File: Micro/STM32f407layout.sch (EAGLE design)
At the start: 68 parts, among them Q1 ASF, Q2 ASV-8, T3 FDN340P, T4 AP1117_LIN_REG

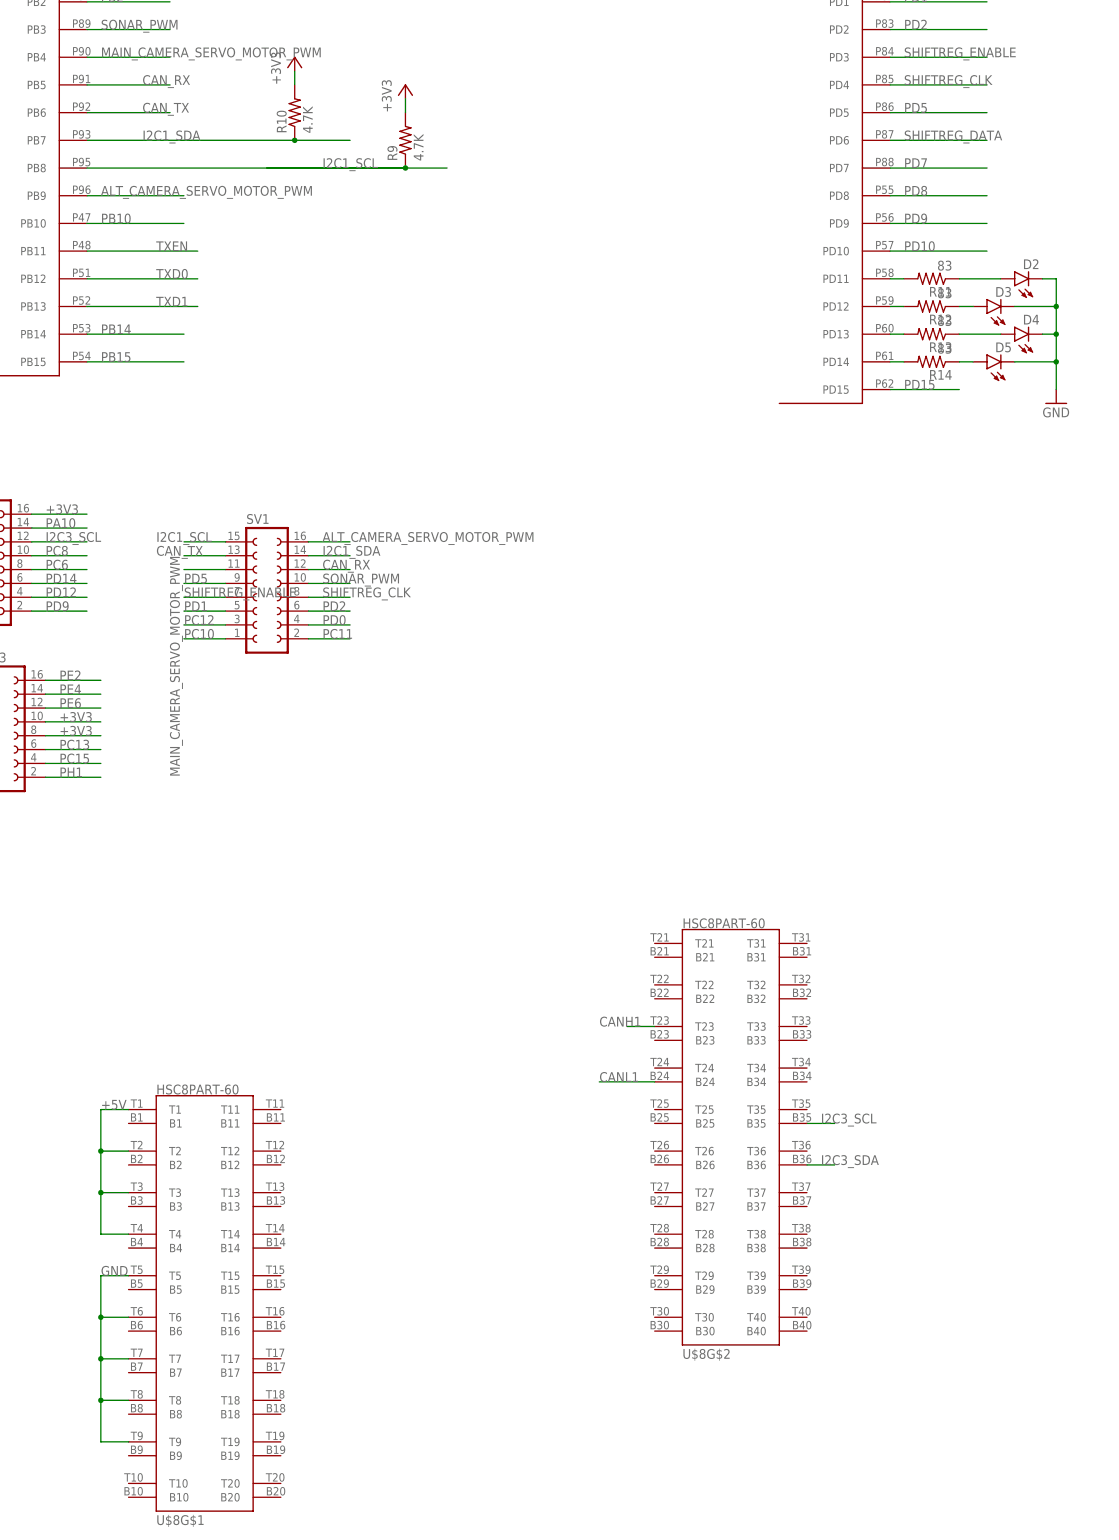
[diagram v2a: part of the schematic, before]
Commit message: Imprved spacing, changed bottom pinouts
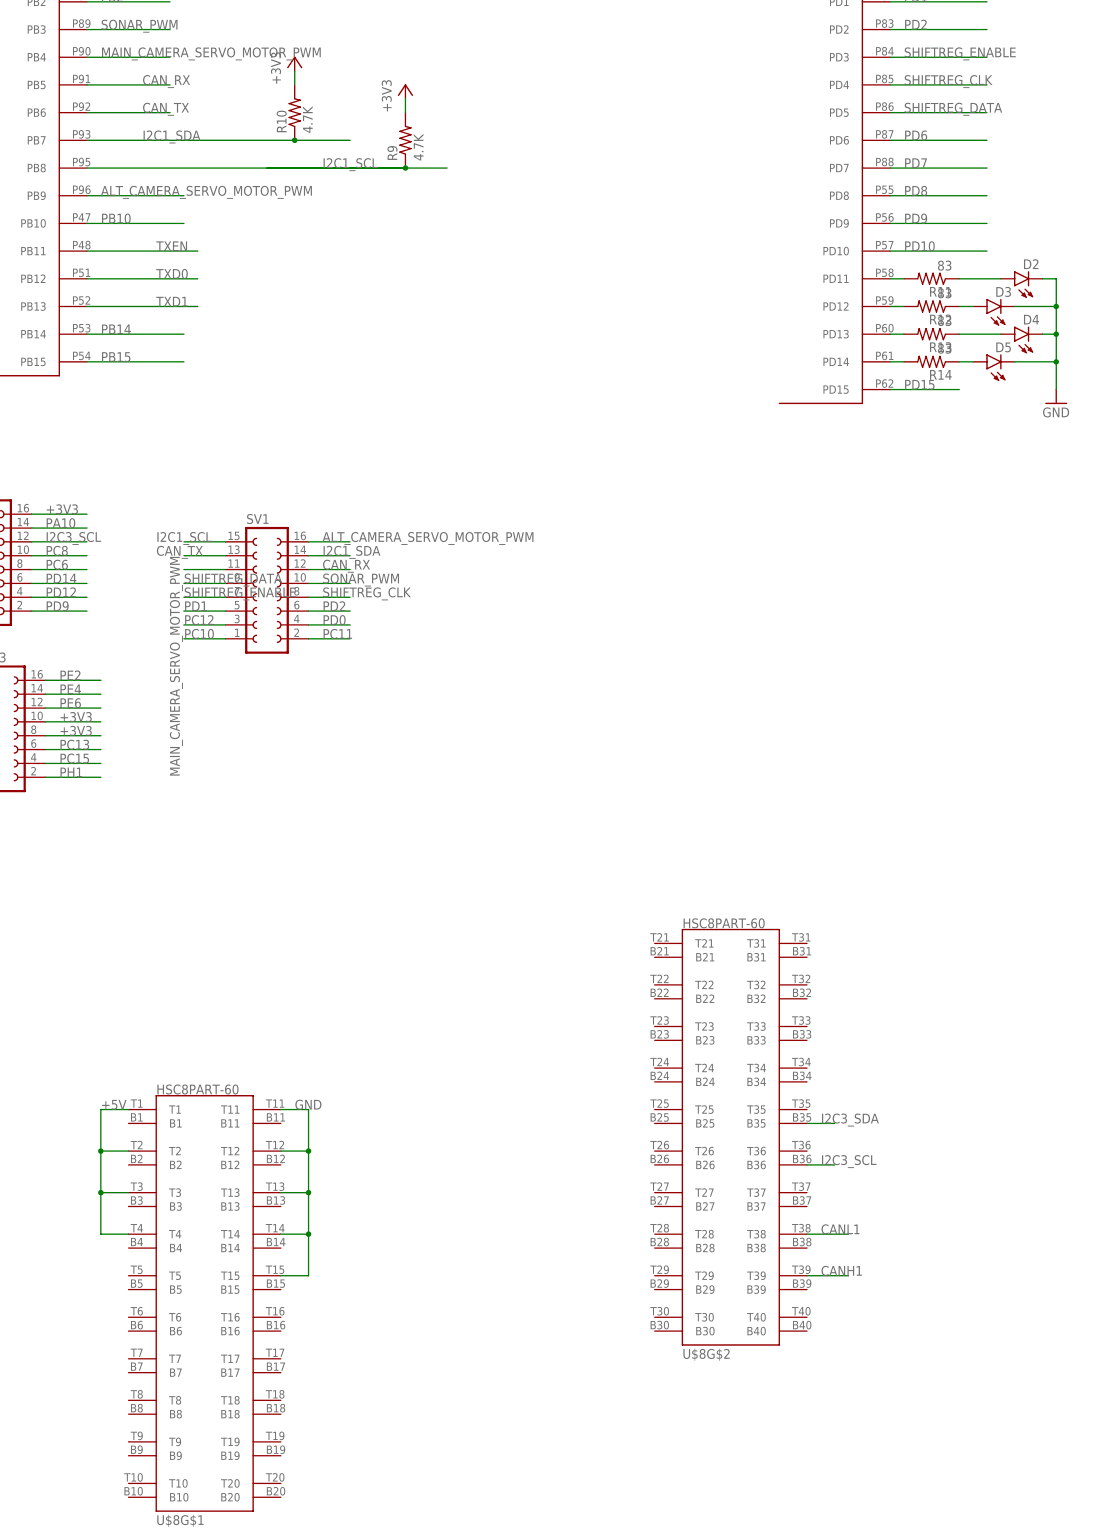
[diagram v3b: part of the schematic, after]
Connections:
- removed net PD5: SV1.9, U$1G$4.PD5
- new net PD6: U$1G$4.PD6
- net CANH1: now also U$8G$2.T39; no longer U$8G$2.T23
- net CANL1: now also U$8G$2.T38; no longer U$8G$2.B24
- net GND: now also U$8G$1.T11, U$8G$1.T12, U$8G$1.T13, U$8G$1.T14, U$8G$1.T15; no longer U$8G$1.T5, U$8G$1.T6, U$8G$1.T7, U$8G$1.T8, U$8G$1.T9
- net I2C3_SCL: now also U$8G$2.B36; no longer U$8G$2.B35
- net I2C3_SDA: now also U$8G$2.B35; no longer U$8G$2.B36
- net SHIFTREG_DATA: now also SV1.9, U$1G$4.PD5; no longer U$1G$4.PD6

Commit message: Fixed DRC Errors, Began fixing other problems
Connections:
- removed net PC11: SV1.2, U$1G$3.PC11
- new net TEMP_BACKUP: SV1.2, U$1G$3.PC11, U$8G$2.T25
- net +5V: now also U$8G$1.T5, U$8G$1.T6; no longer U$8G$1.T1, U$8G$1.T2
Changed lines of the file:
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@@
 </segment>
 <segment>
-<pinref part="U$8" gate="G$1" pin="T1"/>
-<wire x1="447.04" y1="139.7" x2="441.96" y2="139.7" width="0.1524" layer="91"/>
-<label x="441.96" y="139.7" size="1.778" layer="95"/>
-<wire x1="441.96" y1="139.7" x2="441.96" y2="132.08" width="0.1524" layer="91"/>
-<pinref part="U$8" gate="G$1" pin="T2"/>
-<wire x1="441.96" y1="132.08" x2="447.04" y2="132.08" width="0.1524" layer="91"/>
-<wire x1="441.96" y1="132.08" x2="441.96" y2="124.46" width="0.1524" layer="91"/>
-<junction x="441.96" y="132.08"/>
+<label x="441.96" y="124.46" size="1.778" layer="95"/>
 <pinref part="U$8" gate="G$1" pin="T3"/>
 <wire x1="441.96" y1="124.46" x2="447.04" y2="124.46" width="0.1524" layer="91"/>
 <wire x1="441.96" y1="124.46" x2="441.96" y2="116.84" width="0.1524" layer="91"/>
-<junction x="441.96" y="124.46"/>
 <pinref part="U$8" gate="G$1" pin="T4"/>
 <wire x1="441.96" y1="116.84" x2="447.04" y2="116.84" width="0.1524" layer="91"/>
+<wire x1="441.96" y1="116.84" x2="441.96" y2="109.22" width="0.1524" layer="91"/>
+<junction x="441.96" y="116.84"/>
+<pinref part="U$8" gate="G$1" pin="T5"/>
+<wire x1="441.96" y1="109.22" x2="447.04" y2="109.22" width="0.1524" layer="91"/>
+<wire x1="441.96" y1="109.22" x2="441.96" y2="101.6" width="0.1524" layer="91"/>
+<junction x="441.96" y="109.22"/>
+<pinref part="U$8" gate="G$1" pin="T6"/>
+<wire x1="441.96" y1="101.6" x2="447.04" y2="101.6" width="0.1524" layer="91"/>
 </segment>
 </net>
@@
 </segment>
 </net>
-<net name="PC11" class="0">
+<net name="TEMP_BACKUP" class="0">
 <segment>
 <pinref part="SV1" gate="G$1" pin="2"/>
@@
 <label x="586.74" y="454.66" size="1.778" layer="95"/>
 </segment>
-</net>
+<segment>
+<pinref part="U$8" gate="G$2" pin="T25"/>
+<wire x1="543.56" y1="139.7" x2="535.94" y2="139.7" width="0.1524" layer="91"/>
+<label x="528.32" y="139.7" size="1.778" layer="95"/>
+</segment>
+</net>

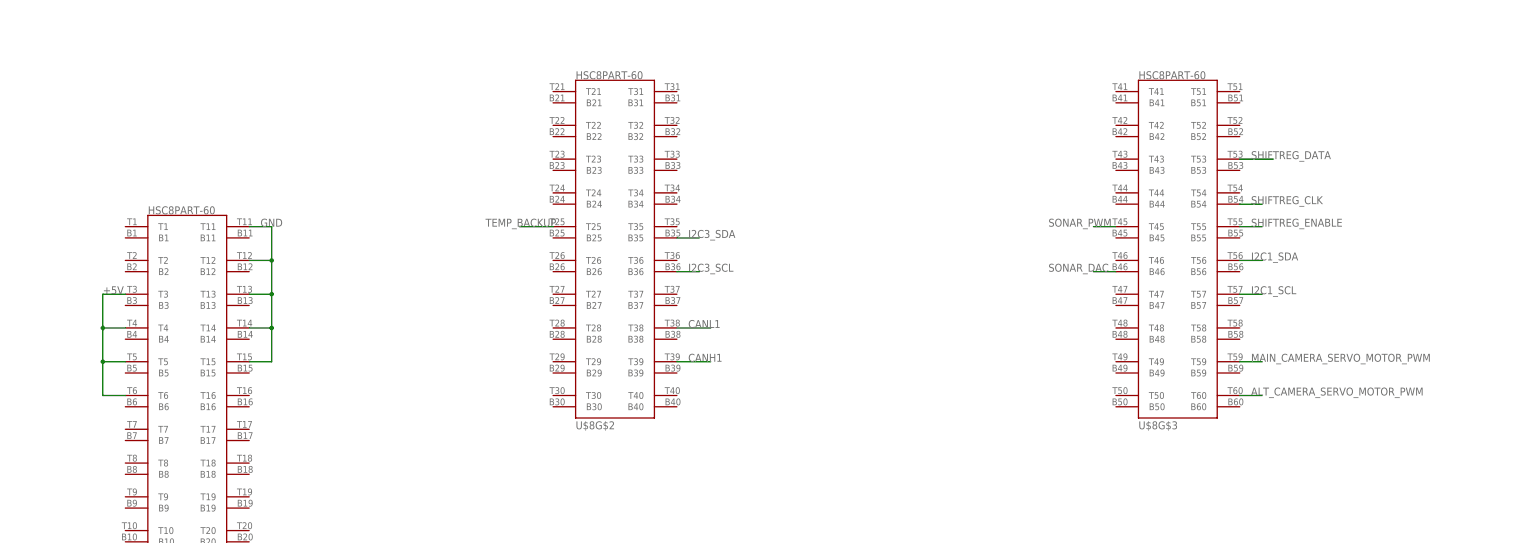
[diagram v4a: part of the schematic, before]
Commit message: Fixed some wiring on the microboard
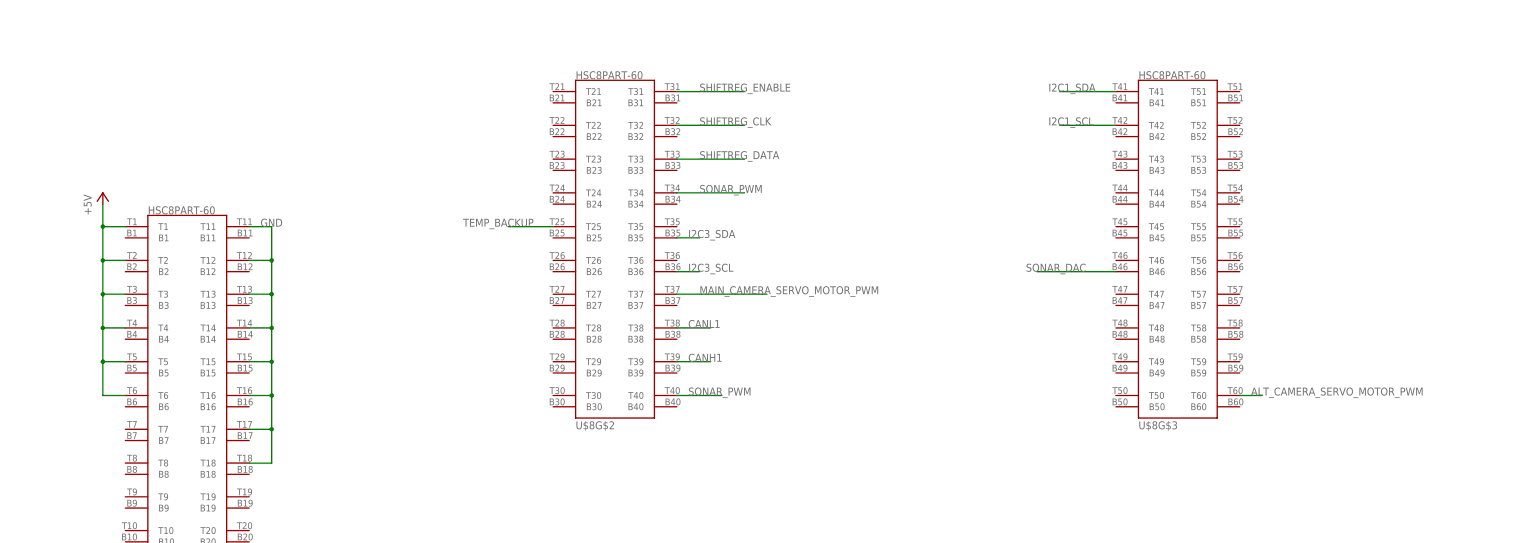
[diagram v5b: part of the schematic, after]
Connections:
- net +5V: now also U$8G$1.T1, U$8G$1.T2
- net GND: now also U$8G$1.T16, U$8G$1.T17, U$8G$1.T18
- net I2C1_SCL: now also U$8G$3.T42; no longer U$8G$3.T57
- net I2C1_SDA: now also U$8G$3.T41; no longer U$8G$3.T56
- net MAIN_CAMERA_SERVO_MOTOR_PWM: now also U$8G$2.T37; no longer U$8G$3.T59
- net SHIFTREG_CLK: now also U$8G$2.T32; no longer U$8G$3.B54
- net SHIFTREG_DATA: now also U$8G$2.T33; no longer U$8G$3.T53
- net SHIFTREG_ENABLE: now also U$8G$2.T31; no longer U$8G$3.T55
- net SONAR_PWM: now also U$8G$2.T34, U$8G$2.T40; no longer U$8G$3.T45
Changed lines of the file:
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@@
 <layers>
 <layer number="1" name="Top" color="4" fill="1" visible="no" active="no"/>
+<layer number="2" name="Route2" color="1" fill="3" visible="no" active="no"/>
+<layer number="3" name="Route3" color="4" fill="3" visible="no" active="no"/>
+<layer number="4" name="Route4" color="1" fill="4" visible="no" active="no"/>
+<layer number="5" name="Route5" color="4" fill="4" visible="no" active="no"/>
+<layer number="6" name="Route6" color="1" fill="8" visible="no" active="no"/>
+<layer number="7" name="Route7" color="4" fill="8" visible="no" active="no"/>
+<layer number="8" name="Route8" color="1" fill="2" visible="no" active="no"/>
+<layer number="9" name="Route9" color="4" fill="2" visible="no" active="no"/>
+<layer number="10" name="Route10" color="1" fill="7" visible="no" active="no"/>
+<layer number="11" name="Route11" color="4" fill="7" visible="no" active="no"/>
+<layer number="12" name="Route12" color="1" fill="5" visible="no" active="no"/>
+<layer number="13" name="Route13" color="4" fill="5" visible="no" active="no"/>
+<layer number="14" name="Route14" color="1" fill="6" visible="no" active="no"/>
+<layer number="15" name="Route15" color="4" fill="6" visible="no" active="no"/>
 <layer number="16" name="Bottom" color="1" fill="1" visible="no" active="no"/>
 <layer number="17" name="Pads" color="2" fill="1" visible="no" active="no"/>
@@
 <part name="+3V20" library="supply1" deviceset="+3V3" device=""/>
 <part name="U$8" library="Connectors" deviceset="HSC8PART-60" device=""/>
+<part name="P+1" library="supply1" deviceset="+5V" device=""/>
 </parts>
 <sheets>
@@
 <instance part="U$8" gate="G$2" x="556.26" y="134.62"/>
 <instance part="U$8" gate="G$3" x="683.26" y="134.62"/>
+<instance part="P+1" gate="1" x="441.96" y="147.32"/>
 </instances>
 <busses>
@@
 <junction x="480.06" y="116.84"/>
 <label x="477.52" y="139.7" size="1.778" layer="95"/>
+<wire x1="480.06" y1="109.22" x2="480.06" y2="101.6" width="0.1524" layer="91"/>
+<junction x="480.06" y="109.22"/>
+<pinref part="U$8" gate="G$1" pin="T16"/>
+<wire x1="480.06" y1="101.6" x2="474.98" y2="101.6" width="0.1524" layer="91"/>
+<wire x1="480.06" y1="101.6" x2="480.06" y2="93.98" width="0.1524" layer="91"/>
+<junction x="480.06" y="101.6"/>
+<pinref part="U$8" gate="G$1" pin="T17"/>
+<wire x1="480.06" y1="93.98" x2="474.98" y2="93.98" width="0.1524" layer="91"/>
+<wire x1="480.06" y1="93.98" x2="480.06" y2="86.36" width="0.1524" layer="91"/>
+<junction x="480.06" y="93.98"/>
+<pinref part="U$8" gate="G$1" pin="T18"/>
+<wire x1="480.06" y1="86.36" x2="474.98" y2="86.36" width="0.1524" layer="91"/>
 </segment>
 </net>
@@
 </segment>
 <segment>
-<label x="441.96" y="124.46" size="1.778" layer="95"/>
-<pinref part="U$8" gate="G$1" pin="T3"/>
-<wire x1="441.96" y1="124.46" x2="447.04" y2="124.46" width="0.1524" layer="91"/>
-<wire x1="441.96" y1="124.46" x2="441.96" y2="116.84" width="0.1524" layer="91"/>
 <pinref part="U$8" gate="G$1" pin="T4"/>
 <wire x1="441.96" y1="116.84" x2="447.04" y2="116.84" width="0.1524" layer="91"/>
@@
 <pinref part="U$8" gate="G$1" pin="T6"/>
 <wire x1="441.96" y1="101.6" x2="447.04" y2="101.6" width="0.1524" layer="91"/>
+<wire x1="441.96" y1="116.84" x2="441.96" y2="124.46" width="0.1524" layer="91"/>
+<pinref part="U$8" gate="G$1" pin="T2"/>
+<wire x1="441.96" y1="124.46" x2="441.96" y2="132.08" width="0.1524" layer="91"/>
+<wire x1="441.96" y1="132.08" x2="447.04" y2="132.08" width="0.1524" layer="91"/>
+<wire x1="441.96" y1="132.08" x2="441.96" y2="139.7" width="0.1524" layer="91"/>
+<junction x="441.96" y="132.08"/>
+<pinref part="U$8" gate="G$1" pin="T1"/>
+<wire x1="441.96" y1="139.7" x2="447.04" y2="139.7" width="0.1524" layer="91"/>
+<pinref part="P+1" gate="1" pin="+5V"/>
+<wire x1="441.96" y1="139.7" x2="441.96" y2="144.78" width="0.1524" layer="91"/>
+<junction x="441.96" y="139.7"/>
+<pinref part="U$8" gate="G$1" pin="T3"/>
+<wire x1="441.96" y1="124.46" x2="447.04" y2="124.46" width="0.1524" layer="91"/>
+<junction x="441.96" y="124.46"/>
 </segment>
 </net>
@@
 </segment>
 <segment>
-<pinref part="U$8" gate="G$3" pin="T45"/>
-<wire x1="670.56" y1="139.7" x2="665.48" y2="139.7" width="0.1524" layer="91"/>
-<label x="655.32" y="139.7" size="1.778" layer="95"/>
-</segment>
-</net>
-<net name="SONAR_DAC" class="0">
-<segment>
-<pinref part="U$1" gate="G$1" pin="PA4"/>
-<wire x1="439.42" y1="490.22" x2="452.12" y2="490.22" width="0.1524" layer="91"/>
-<label x="441.96" y="490.22" size="1.778" layer="95"/>
-</segment>
-<segment>
-<pinref part="U$8" gate="G$3" pin="B46"/>
-<wire x1="670.56" y1="129.54" x2="665.48" y2="129.54" width="0.1524" layer="91"/>
-<label x="655.32" y="129.54" size="1.778" layer="95"/>
+<pinref part="U$8" gate="G$2" pin="T34"/>
+<wire x1="571.5" y1="147.32" x2="586.74" y2="147.32" width="0.1524" layer="91"/>
+<label x="576.58" y="147.32" size="1.778" layer="95"/>
+</segment>
+<segment>
+<pinref part="U$8" gate="G$2" pin="T40"/>
+<wire x1="571.5" y1="101.6" x2="581.66" y2="101.6" width="0.1524" layer="91"/>
+<label x="574.04" y="101.6" size="1.778" layer="95"/>
 </segment>
 </net>
@@
 </segment>
 <segment>
-<pinref part="U$8" gate="G$3" pin="T56"/>
-<wire x1="698.5" y1="132.08" x2="703.58" y2="132.08" width="0.1524" layer="91"/>
-<label x="701.04" y="132.08" size="1.778" layer="95"/>
+<pinref part="U$8" gate="G$3" pin="T41"/>
+<wire x1="670.56" y1="170.18" x2="657.86" y2="170.18" width="0.1524" layer="91"/>
+<label x="655.32" y="170.18" size="1.778" layer="95"/>
 </segment>
 </net>
@@
 </segment>
 <segment>
-<pinref part="U$8" gate="G$3" pin="T57"/>
-<wire x1="698.5" y1="124.46" x2="703.58" y2="124.46" width="0.1524" layer="91"/>
-<label x="701.04" y="124.46" size="1.778" layer="95"/>
+<pinref part="U$8" gate="G$3" pin="T42"/>
+<wire x1="670.56" y1="162.56" x2="657.86" y2="162.56" width="0.1524" layer="91"/>
+<label x="655.32" y="162.56" size="1.778" layer="95"/>
 </segment>
 </net>
@@
 </segment>
 <segment>
-<pinref part="U$8" gate="G$3" pin="T59"/>
-<wire x1="698.5" y1="109.22" x2="703.58" y2="109.22" width="0.1524" layer="91"/>
-<label x="701.04" y="109.22" size="1.778" layer="95"/>
+<pinref part="U$8" gate="G$2" pin="T37"/>
+<wire x1="571.5" y1="124.46" x2="591.82" y2="124.46" width="0.1524" layer="91"/>
+<label x="576.58" y="124.46" size="1.778" layer="95"/>
 </segment>
 </net>
@@
 </segment>
 <segment>
-<pinref part="U$8" gate="G$3" pin="B54"/>
-<wire x1="698.5" y1="144.78" x2="703.58" y2="144.78" width="0.1524" layer="91"/>
-<label x="701.04" y="144.78" size="1.778" layer="95"/>
+<pinref part="U$8" gate="G$2" pin="T32"/>
+<wire x1="571.5" y1="162.56" x2="586.74" y2="162.56" width="0.1524" layer="91"/>
+<label x="576.58" y="162.56" size="1.778" layer="95"/>
 </segment>
 </net>
@@
 <segment>
 <pinref part="U$8" gate="G$2" pin="T25"/>
-<wire x1="543.56" y1="139.7" x2="535.94" y2="139.7" width="0.1524" layer="91"/>
-<label x="528.32" y="139.7" size="1.778" layer="95"/>
+<wire x1="543.56" y1="139.7" x2="533.4" y2="139.7" width="0.1524" layer="91"/>
+<label x="523.24" y="139.7" size="1.778" layer="95"/>
 </segment>
 </net>
@@
 </segment>
 <segment>
-<pinref part="U$8" gate="G$3" pin="T55"/>
-<wire x1="698.5" y1="139.7" x2="703.58" y2="139.7" width="0.1524" layer="91"/>
-<label x="701.04" y="139.7" size="1.778" layer="95"/>
+<pinref part="U$8" gate="G$2" pin="T31"/>
+<wire x1="571.5" y1="170.18" x2="586.74" y2="170.18" width="0.1524" layer="91"/>
+<label x="576.58" y="170.18" size="1.778" layer="95"/>
 </segment>
 </net>
@@
 </segment>
 <segment>
-<pinref part="U$8" gate="G$3" pin="T53"/>
-<wire x1="698.5" y1="154.94" x2="706.12" y2="154.94" width="0.1524" layer="91"/>
-<label x="701.04" y="154.94" size="1.778" layer="95"/>
+<pinref part="U$8" gate="G$2" pin="T33"/>
+<wire x1="571.5" y1="154.94" x2="586.74" y2="154.94" width="0.1524" layer="91"/>
+<label x="576.58" y="154.94" size="1.778" layer="95"/>
 </segment>
 </net>
@@
 </segment>
 </net>
+<net name="SONAR_DAC" class="0">
+<segment>
+<pinref part="U$8" gate="G$3" pin="B46"/>
+<wire x1="670.56" y1="129.54" x2="652.78" y2="129.54" width="0.1524" layer="91"/>
+<label x="650.24" y="129.54" size="1.778" layer="95"/>
+</segment>
+<segment>
+<pinref part="U$1" gate="G$1" pin="PA4"/>
+<wire x1="439.42" y1="490.22" x2="452.12" y2="490.22" width="0.1524" layer="91"/>
+<label x="441.96" y="490.22" size="1.778" layer="95"/>
+</segment>
+</net>
